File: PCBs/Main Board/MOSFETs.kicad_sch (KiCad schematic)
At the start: 24 parts, among them J1 S2P-VHLFSN, J2 S2P-VHLFSN, J3 S2P-VHLFSN, J4 S2P-VHLFSN, J5 S2P-VHLFSN, Q1 FQP30N06L, Q2 FQP30N06L, Q3 FQP30N06L, Q4 FQP30N06L, Q5 FQP30N06L

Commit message: Remove steppers, add OLED
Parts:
- gave numbers to parts that had none: 4
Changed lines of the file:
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@@
   (symbol (lib_id "power:GND") (at 210.82 96.52 0) (unit 1)
     (in_bom yes) (on_board yes) (fields_autoplaced)
-    (property "Reference" "#PWR?" (id 0) (at 210.82 102.87 0)
+    (property "Reference" "#PWR012" (id 0) (at 210.82 102.87 0)
       (effects (font (size 1.27 1.27)) hide)
     )
@@
   (symbol (lib_id "Hydro_Library:FQP30N06L") (at 208.28 86.36 0) (unit 1)
     (in_bom yes) (on_board yes) (fields_autoplaced)
-    (property "Reference" "Q?" (id 0) (at 214.63 85.0899 0)
+    (property "Reference" "Q6" (id 0) (at 214.63 85.0899 0)
       (effects (font (size 1.27 1.27)) (justify left))
     )
@@
   (symbol (lib_id "power:GND") (at 81.28 95.25 0) (unit 1)
     (in_bom yes) (on_board yes) (fields_autoplaced)
-    (property "Reference" "#PWR?" (id 0) (at 81.28 101.6 0)
+    (property "Reference" "#PWR03" (id 0) (at 81.28 101.6 0)
       (effects (font (size 1.27 1.27)) hide)
     )
@@
   (symbol (lib_id "Diode:1N4007") (at 207.01 78.74 0) (unit 1)
     (in_bom yes) (on_board yes) (fields_autoplaced)
-    (property "Reference" "D?" (id 0) (at 207.01 72.39 0))
+    (property "Reference" "D6" (id 0) (at 207.01 72.39 0))
     (property "Value" "1N4007" (id 1) (at 207.01 74.93 0))
     (property "Footprint" "Diode_THT:D_DO-41_SOD81_P10.16mm_Horizontal" (id 2) (at 207.01 83.185 0)
@@
   (symbol (lib_id "S2P-VH(LF)(SN):S2P-VHLFSN") (at 208.28 72.39 90) (unit 1)
     (in_bom yes) (on_board yes) (fields_autoplaced)
-    (property "Reference" "J?" (id 0) (at 214.63 62.23 90)
+    (property "Reference" "J6" (id 0) (at 214.63 62.23 90)
       (effects (font (size 1.524 1.524)) (justify right))
     )
@@
   (symbol (lib_id "power:GND") (at 52.07 92.71 0) (unit 1)
     (in_bom yes) (on_board yes) (fields_autoplaced)
-    (property "Reference" "#PWR01" (id 0) (at 52.07 99.06 0)
+    (property "Reference" "#PWR02" (id 0) (at 52.07 99.06 0)
       (effects (font (size 1.27 1.27)) hide)
     )
@@
   (symbol (lib_id "power:GND") (at 44.45 95.25 0) (unit 1)
     (in_bom yes) (on_board yes) (fields_autoplaced)
-    (property "Reference" "#PWR?" (id 0) (at 44.45 101.6 0)
+    (property "Reference" "#PWR01" (id 0) (at 44.45 101.6 0)
       (effects (font (size 1.27 1.27)) hide)
     )
@@
   (symbol (lib_id "power:GND") (at 177.8 96.52 0) (unit 1)
     (in_bom yes) (on_board yes) (fields_autoplaced)
-    (property "Reference" "#PWR05" (id 0) (at 177.8 102.87 0)
+    (property "Reference" "#PWR010" (id 0) (at 177.8 102.87 0)
       (effects (font (size 1.27 1.27)) hide)
     )
@@
   (symbol (lib_id "power:GND") (at 109.22 95.25 0) (unit 1)
     (in_bom yes) (on_board yes) (fields_autoplaced)
-    (property "Reference" "#PWR?" (id 0) (at 109.22 101.6 0)
+    (property "Reference" "#PWR05" (id 0) (at 109.22 101.6 0)
       (effects (font (size 1.27 1.27)) hide)
     )
@@
   (symbol (lib_id "power:GND") (at 171.45 93.98 0) (unit 1)
     (in_bom yes) (on_board yes) (fields_autoplaced)
-    (property "Reference" "#PWR?" (id 0) (at 171.45 100.33 0)
+    (property "Reference" "#PWR09" (id 0) (at 171.45 100.33 0)
       (effects (font (size 1.27 1.27)) hide)
     )
@@
   (symbol (lib_id "power:GND") (at 115.57 92.71 0) (unit 1)
     (in_bom yes) (on_board yes) (fields_autoplaced)
-    (property "Reference" "#PWR03" (id 0) (at 115.57 99.06 0)
+    (property "Reference" "#PWR06" (id 0) (at 115.57 99.06 0)
       (effects (font (size 1.27 1.27)) hide)
     )
@@
   (symbol (lib_id "power:GND") (at 204.47 93.98 0) (unit 1)
     (in_bom yes) (on_board yes) (fields_autoplaced)
-    (property "Reference" "#PWR?" (id 0) (at 204.47 100.33 0)
+    (property "Reference" "#PWR011" (id 0) (at 204.47 100.33 0)
       (effects (font (size 1.27 1.27)) hide)
     )
@@
   (symbol (lib_id "power:GND") (at 87.63 92.71 0) (unit 1)
     (in_bom yes) (on_board yes) (fields_autoplaced)
-    (property "Reference" "#PWR02" (id 0) (at 87.63 99.06 0)
+    (property "Reference" "#PWR04" (id 0) (at 87.63 99.06 0)
       (effects (font (size 1.27 1.27)) hide)
     )
@@
   (symbol (lib_id "power:GND") (at 138.43 93.98 0) (unit 1)
     (in_bom yes) (on_board yes) (fields_autoplaced)
-    (property "Reference" "#PWR?" (id 0) (at 138.43 100.33 0)
+    (property "Reference" "#PWR07" (id 0) (at 138.43 100.33 0)
       (effects (font (size 1.27 1.27)) hide)
     )
@@
   (symbol (lib_id "power:GND") (at 144.78 96.52 0) (unit 1)
     (in_bom yes) (on_board yes) (fields_autoplaced)
-    (property "Reference" "#PWR04" (id 0) (at 144.78 102.87 0)
+    (property "Reference" "#PWR08" (id 0) (at 144.78 102.87 0)
       (effects (font (size 1.27 1.27)) hide)
     )
@@
   (symbol (lib_id "Device:R_Small_US") (at 204.47 91.44 0) (unit 1)
     (in_bom yes) (on_board yes)
-    (property "Reference" "R?" (id 0) (at 200.66 91.44 0)
-      (effects (font (size 1.27 1.27)) (justify left))
-    )
+    (property "Reference" "R6" (id 0) (at 200.66 91.44 0)
+      (effects (font (size 1.27 1.27)) (justify left))
+    )

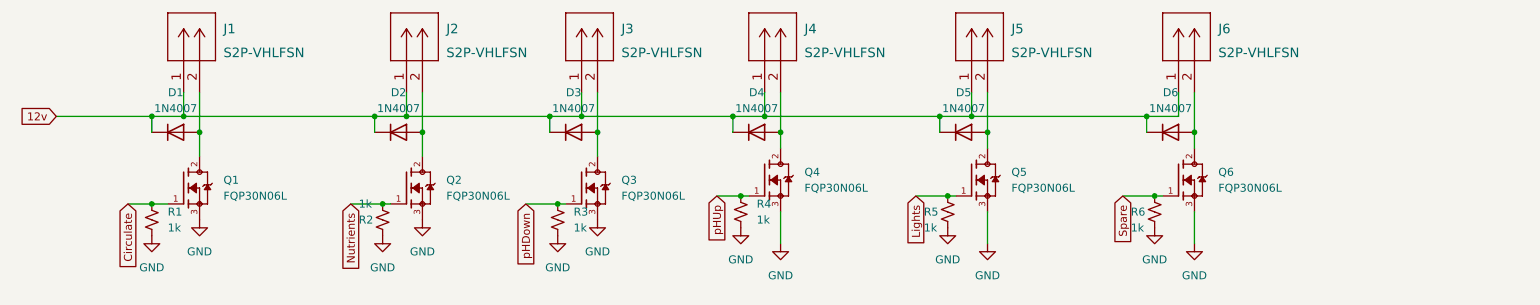
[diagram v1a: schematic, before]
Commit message: Changed some pins
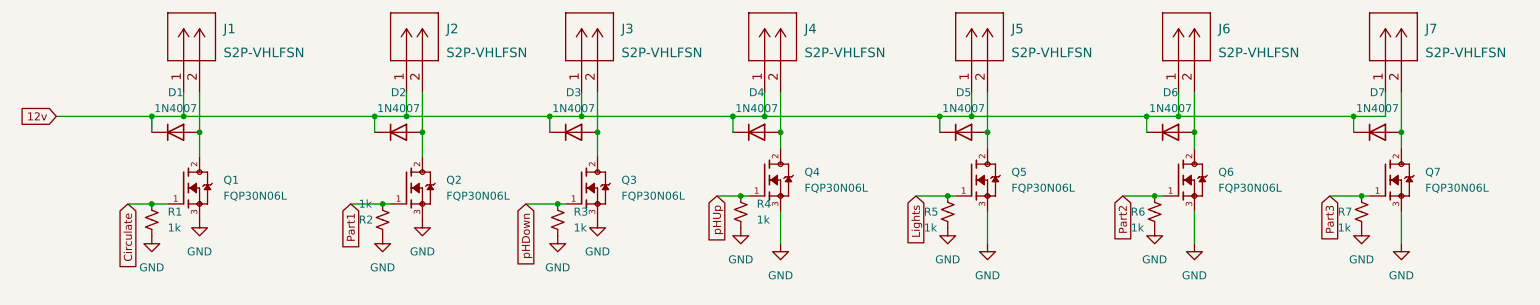
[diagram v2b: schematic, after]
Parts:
- added D7: 1N4007, Diode_THT:D_DO-41_SOD81_P10.16mm_Horizontal, symbol Diode:1N4007
- added J7: S2P-VHLFSN, Hydro:S2P-VHLFSN, symbol S2P-VH(LF)(SN):S2P-VHLFSN
- added Q7: FQP30N06L, TO220V, symbol Hydro_Library:FQP30N06L
- added R7: 1k, Resistor_THT:R_Axial_DIN0207_L6.3mm_D2.5mm_P7.62mm_Horizontal, symbol Device:R_Small_US
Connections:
- net 12v: now also D7.1 (K), J7.1
- net GND: now also Q7.3, R7.2
- net Nutrients renamed Part1
- net Spare renamed Part2
- new net: D7.2 (A), J7.2, Q7.2
- new net Part3: Q7.1, R7.1
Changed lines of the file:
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@@
 (kicad_sch (version 20211123) (generator eeschema)
   (paper "A4")
+  (junction (at 236.22 76.2) (diameter 0) (color 0 0 0 0)
+  )
   (junction (at 210.82 78.74) (diameter 0) (color 0 0 0 0)
   )
@@
   (junction (at 113.03 76.2) (diameter 0) (color 0 0 0 0)
   )
+  (junction (at 237.49 88.9) (diameter 0) (color 0 0 0 0)
+  )
   (junction (at 142.24 76.2) (diameter 0) (color 0 0 0 0)
   )
@@
   (junction (at 87.63 78.74) (diameter 0) (color 0 0 0 0)
   )
+  (junction (at 208.28 76.2) (diameter 0) (color 0 0 0 0)
+  )
   (junction (at 138.43 88.9) (diameter 0) (color 0 0 0 0)
   )
   (junction (at 175.26 76.2) (diameter 0) (color 0 0 0 0)
   )
+  (junction (at 243.84 78.74) (diameter 0) (color 0 0 0 0)
+  )
   (junction (at 80.01 76.2) (diameter 0) (color 0 0 0 0)
   )
@@
     (stroke (width 0) (type default) (color 0 0 0 0))
   )
+  (wire (pts (xy 243.84 96.52) (xy 243.84 91.44))
+    (stroke (width 0) (type default) (color 0 0 0 0))
+  )
   (wire (pts (xy 144.78 78.74) (xy 144.78 81.28))
     (stroke (width 0) (type default) (color 0 0 0 0))
   )
+  (wire (pts (xy 237.49 88.9) (xy 238.76 88.9))
+    (stroke (width 0) (type default) (color 0 0 0 0))
+  )
   (wire (pts (xy 177.8 72.39) (xy 177.8 78.74))
     (stroke (width 0) (type default) (color 0 0 0 0))
@@
     (stroke (width 0) (type default) (color 0 0 0 0))
   )
+  (wire (pts (xy 208.28 76.2) (xy 236.22 76.2))
+    (stroke (width 0) (type default) (color 0 0 0 0))
+  )
   (wire (pts (xy 203.2 76.2) (xy 203.2 78.74))
     (stroke (width 0) (type default) (color 0 0 0 0))
   )
+  (wire (pts (xy 243.84 72.39) (xy 243.84 78.74))
+    (stroke (width 0) (type default) (color 0 0 0 0))
+  )
   (wire (pts (xy 166.37 88.9) (xy 171.45 88.9))
     (stroke (width 0) (type default) (color 0 0 0 0))
@@
     (stroke (width 0) (type default) (color 0 0 0 0))
   )
+  (wire (pts (xy 241.3 72.39) (xy 241.3 76.2))
+    (stroke (width 0) (type default) (color 0 0 0 0))
+  )
   (wire (pts (xy 170.18 76.2) (xy 175.26 76.2))
     (stroke (width 0) (type default) (color 0 0 0 0))
   )
+  (wire (pts (xy 236.22 76.2) (xy 236.22 78.74))
+    (stroke (width 0) (type default) (color 0 0 0 0))
+  )
   (wire (pts (xy 76.2 90.17) (xy 81.28 90.17))
     (stroke (width 0) (type default) (color 0 0 0 0))
@@
     (stroke (width 0) (type default) (color 0 0 0 0))
   )
+  (wire (pts (xy 232.41 88.9) (xy 237.49 88.9))
+    (stroke (width 0) (type default) (color 0 0 0 0))
+  )
   (wire (pts (xy 137.16 76.2) (xy 137.16 78.74))
     (stroke (width 0) (type default) (color 0 0 0 0))
@@
     (stroke (width 0) (type default) (color 0 0 0 0))
   )
+  (wire (pts (xy 236.22 76.2) (xy 241.3 76.2))
+    (stroke (width 0) (type default) (color 0 0 0 0))
+  )
   (wire (pts (xy 115.57 72.39) (xy 115.57 78.74))
     (stroke (width 0) (type default) (color 0 0 0 0))
@@
   )
   (wire (pts (xy 171.45 88.9) (xy 172.72 88.9))
+    (stroke (width 0) (type default) (color 0 0 0 0))
+  )
+  (wire (pts (xy 243.84 78.74) (xy 243.84 81.28))
     (stroke (width 0) (type default) (color 0 0 0 0))
   )
@@
     )
   )
-  (global_label "Spare" (shape input) (at 199.39 88.9 270) (fields_autoplaced)
+  (global_label "Part3" (shape input) (at 232.41 88.9 270) (fields_autoplaced)
     (effects (font (size 1.27 1.27)) (justify right))
-    (property "Intersheet References" "${INTERSHEET_REFS}" (id 0) (at 199.3106 96.6955 90)
+    (property "Intersheet References" "${INTERSHEET_REFS}" (id 0) (at 232.3306 96.4536 90)
+      (effects (font (size 1.27 1.27)) (justify right) hide)
+    )
+  )
+  (global_label "Part2" (shape input) (at 199.39 88.9 270) (fields_autoplaced)
+    (effects (font (size 1.27 1.27)) (justify right))
+    (property "Intersheet References" "${INTERSHEET_REFS}" (id 0) (at 199.3106 96.4536 90)
       (effects (font (size 1.27 1.27)) (justify right) hide)
     )
@@
     )
   )
-  (global_label "Nutrients" (shape input) (at 76.2 90.17 270) (fields_autoplaced)
+  (global_label "Part1" (shape input) (at 76.2 90.17 270) (fields_autoplaced)
     (effects (font (size 1.27 1.27)) (justify right))
-    (property "Intersheet References" "${INTERSHEET_REFS}" (id 0) (at 76.1206 101.1707 90)
+    (property "Intersheet References" "${INTERSHEET_REFS}" (id 0) (at 76.1206 97.7236 90)
       (effects (font (size 1.27 1.27)) (justify right) hide)
     )
@@
     (pin "1")
   )
+  (symbol (lib_id "Diode:1N4007") (at 240.03 78.74 0) (unit 1)
+    (in_bom yes) (on_board yes) (fields_autoplaced)
+    (property "Reference" "D7" (id 0) (at 240.03 72.39 0))
+    (property "Value" "1N4007" (id 1) (at 240.03 74.93 0))
+    (property "Footprint" "Diode_THT:D_DO-41_SOD81_P10.16mm_Horizontal" (id 2) (at 240.03 83.185 0)
+      (effects (font (size 1.27 1.27)) hide)
+    )
+    (property "Datasheet" "http://www.vishay.com/docs/88503/1n4001.pdf" (id 3) (at 240.03 78.74 0)
+      (effects (font (size 1.27 1.27)) hide)
+    )
+    (pin "1")
+    (pin "2")
+  )
   (symbol (lib_id "Diode:1N4007") (at 207.01 78.74 0) (unit 1)
     (in_bom yes) (on_board yes) (fields_autoplaced)
@@
     (pin "2")
   )
+  (symbol (lib_id "Hydro_Library:FQP30N06L") (at 241.3 86.36 0) (unit 1)
+    (in_bom yes) (on_board yes) (fields_autoplaced)
+    (property "Reference" "Q7" (id 0) (at 247.65 85.0899 0)
+      (effects (font (size 1.27 1.27)) (justify left))
+    )
+    (property "Value" "FQP30N06L" (id 1) (at 247.65 87.6299 0)
+      (effects (font (size 1.27 1.27)) (justify left))
+    )
+    (property "Footprint" "TO220V" (id 2) (at 241.3 86.36 0)
+      (effects (font (size 1.27 1.27)) (justify bottom) hide)
+    )
+    (property "Datasheet" "" (id 3) (at 241.3 86.36 0)
+      (effects (font (size 1.27 1.27)) hide)
+    )
+    (pin "1")
+    (pin "2")
+    (pin "3")
+  )
   (symbol (lib_id "power:GND") (at 52.07 92.71 0) (unit 1)
     (in_bom yes) (on_board yes) (fields_autoplaced)
@@
     (pin "2")
     (pin "3")
+  )
+  (symbol (lib_id "Device:R_Small_US") (at 237.49 91.44 0) (unit 1)
+    (in_bom yes) (on_board yes)
+    (property "Reference" "R7" (id 0) (at 233.68 91.44 0)
+      (effects (font (size 1.27 1.27)) (justify left))
+    )
+    (property "Value" "1k" (id 1) (at 233.68 93.98 0)
+      (effects (font (size 1.27 1.27)) (justify left))
+    )
+    (property "Footprint" "Resistor_THT:R_Axial_DIN0207_L6.3mm_D2.5mm_P7.62mm_Horizontal" (id 2) (at 237.49 91.44 0)
+      (effects (font (size 1.27 1.27)) hide)
+    )
+    (property "Datasheet" "~" (id 3) (at 237.49 91.44 0)
+      (effects (font (size 1.27 1.27)) hide)
+    )
+    (pin "1")
+    (pin "2")
   )
   (symbol (lib_id "Diode:1N4007") (at 83.82 78.74 0) (unit 1)
@@
     (pin "2")
   )
+  (symbol (lib_id "S2P-VH(LF)(SN):S2P-VHLFSN") (at 241.3 72.39 90) (unit 1)
+    (in_bom yes) (on_board yes) (fields_autoplaced)
+    (property "Reference" "J7" (id 0) (at 247.65 62.23 90)
+      (effects (font (size 1.524 1.524)) (justify right))
+    )
+    (property "Value" "S2P-VHLFSN" (id 1) (at 247.65 66.04 90)
+      (effects (font (size 1.524 1.524)) (justify right))
+    )
+    (property "Footprint" "Hydro:S2P-VHLFSN" (id 2) (at 242.824 62.23 0)
+      (effects (font (size 1.524 1.524)) hide)
+    )
+    (property "Datasheet" "" (id 3) (at 241.3 72.39 0)
+      (effects (font (size 1.524 1.524)))
+    )
+    (pin "1")
+    (pin "2")
+  )
   (symbol (lib_id "S2P-VH(LF)(SN):S2P-VHLFSN") (at 142.24 72.39 90) (unit 1)
     (in_bom yes) (on_board yes) (fields_autoplaced)
@@
     (pin "1")
     (pin "2")
+  )
+  (symbol (lib_id "power:GND") (at 243.84 96.52 0) (unit 1)
+    (in_bom yes) (on_board yes) (fields_autoplaced)
+    (property "Reference" "#PWR014" (id 0) (at 243.84 102.87 0)
+      (effects (font (size 1.27 1.27)) hide)
+    )
+    (property "Value" "GND" (id 1) (at 243.84 101.6 0))
+    (property "Footprint" "" (id 2) (at 243.84 96.52 0)
+      (effects (font (size 1.27 1.27)) hide)
+    )
+    (property "Datasheet" "" (id 3) (at 243.84 96.52 0)
+      (effects (font (size 1.27 1.27)) hide)
+    )
+    (pin "1")
   )
   (symbol (lib_id "power:GND") (at 44.45 95.25 0) (unit 1)
@@
     (pin "2")
   )
+  (symbol (lib_id "power:GND") (at 237.49 93.98 0) (unit 1)
+    (in_bom yes) (on_board yes) (fields_autoplaced)
+    (property "Reference" "#PWR013" (id 0) (at 237.49 100.33 0)
+      (effects (font (size 1.27 1.27)) hide)
+    )
+    (property "Value" "GND" (id 1) (at 237.49 99.06 0))
+    (property "Footprint" "" (id 2) (at 237.49 93.98 0)
+      (effects (font (size 1.27 1.27)) hide)
+    )
+    (property "Datasheet" "" (id 3) (at 237.49 93.98 0)
+      (effects (font (size 1.27 1.27)) hide)
+    )
+    (pin "1")
+  )
   (symbol (lib_id "Hydro_Library:FQP30N06L") (at 175.26 86.36 0) (unit 1)
